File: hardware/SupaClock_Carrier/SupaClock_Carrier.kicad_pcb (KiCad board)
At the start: 2 copper layers, 67 x 85 mm, 25 parts, among them J11 AD8232_SparkFun, J12_LA1 ECG_LA_pad_M3, J12_RA1 ECG_RA_pad_M3, J12_RL1 ECG_RL_pad_M3, J13 AD8232_Pads_RA_LA_RL, J14 MAX30102_bot, J15 XIAO_BAT_Wires, J3 MAX30102_top, J4 MAX30205_8pad, J5 BMI160_7p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

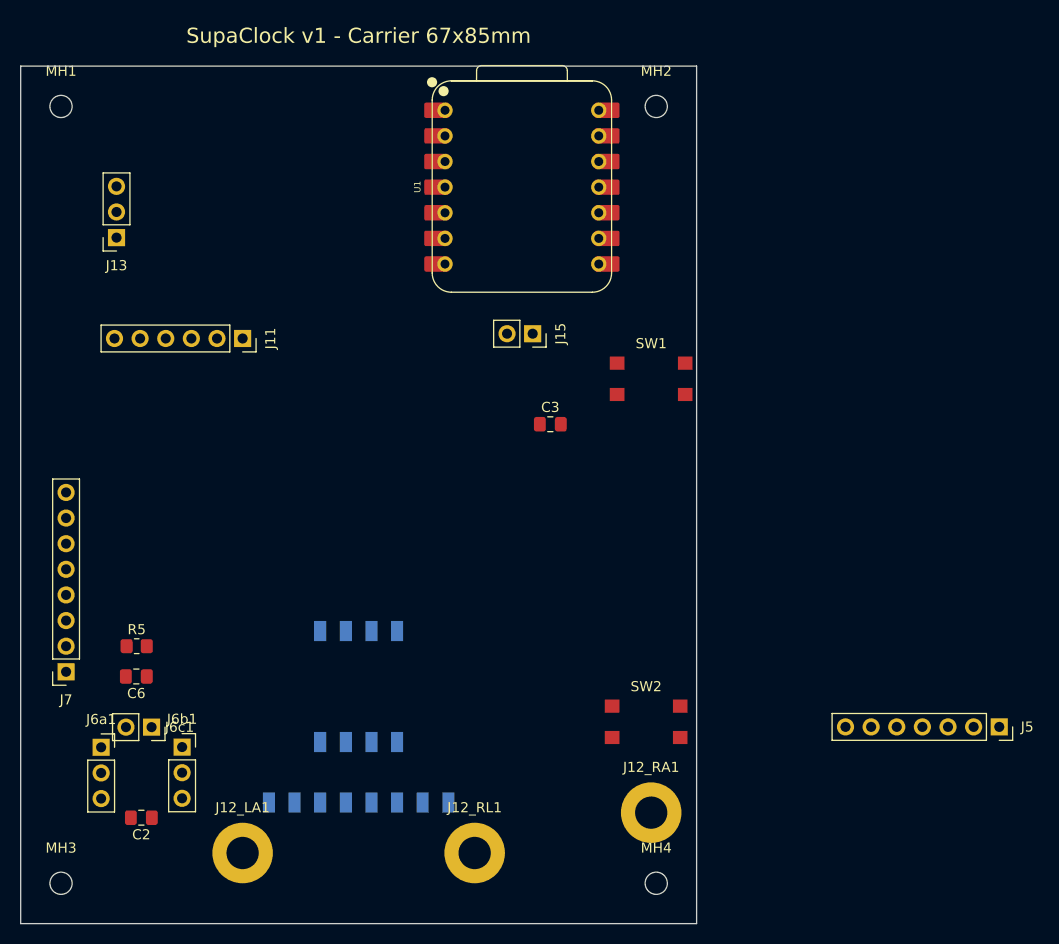
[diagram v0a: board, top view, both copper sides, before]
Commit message: feat: Update SupaClock Carrier project settings and add tuning profiles
- Disabled default application for footprint barcodes and dimensions.
- Introduced new warnings for footprint symbol field mismatches and missing tuning profiles.
- Added support for tuning profiles in design settings.
- Updated IPC2581 settings with a new schematic revision field.
- Enhanced error handling for various design rule checks.
- Incremented project version to 5 and added tuning profiles metadata.
- Included new annotation settings and top-level sheet information in schematic.
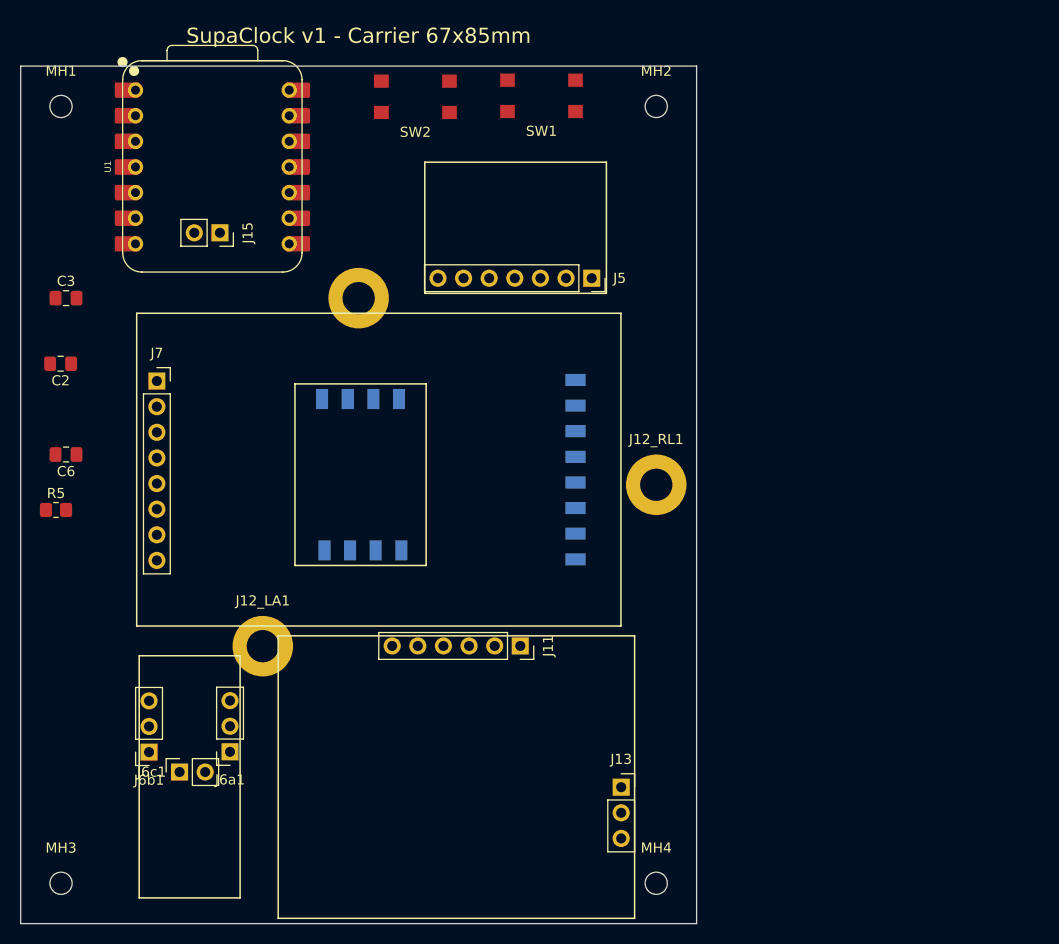
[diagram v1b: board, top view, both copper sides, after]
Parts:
- J12_RA1: moved to B.Cu
- moved J13 74.0 mm to (105.5, 107.5), turned to 0 degrees
- moved SW2 66.0 mm to (85.1, 39.0), turned to 180 degrees
- moved J5 60.1 mm to (102.6, 57.0)
- moved J12_RA1 58.7 mm to (79.5, 59.0), turned to 180 degrees
- moved C3 49.6 mm to (50.5, 59.0)
- moved C2 45.7 mm to (50.0, 65.5)
- moved J4 41.4 mm to (96.0, 76.0), turned to -90 degrees
- moved J11 41.1 mm to (95.5, 93.5)
- moved J12_RL1 40.7 mm to (109.0, 77.5)
- moved J14 34.0 mm to (79.7, 68.0)
- moved J15 32.6 mm to (65.8, 52.5)
- moved U1 30.7 mm to (65.0, 46.0)
- moved J7 30.2 mm to (59.5, 67.2), turned to 0 degrees
- moved SW1 30.1 mm to (97.6, 39.0), turned to 180 degrees
- moved C6 23.1 mm to (50.5, 74.5)
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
